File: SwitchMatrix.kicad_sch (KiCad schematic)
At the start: 130 parts, among them K1 Home, K10 A, K11 Z, K12 Alt, K13 W, K14 S, K15 X, K16 Super, K17 E, K18 D, K19 C, K2 End, K20 &dArr;, K21 R, K22 F, K23 V, K24 T, K25 G, K26 B, K27 Blank, K28 Y, K29 H, K3 Vol +, K30 N, K31 U, K32 J, K33 M, K34 &uArr;, K35 I, K36 K, K37 ,, K38 Alt, K39 O, K4 Vol -, K40 L, K41 ., K42 Fn, K43 P, K44 ;, K45 /, K46 Back Space, K47 ', K48 Shift, K49 &larr;, K5 Tab, K50 Delete, K51 Return, K52 &uarr;, K53 &darr;, K54 &rarr;, K55 1, K56 4, K57 7, K58 2, K59 5, K6 Esc, K60 8, K61 0, K62 3, K63 6, K64 9, K65 Enter, K7 Shift, K8 Ctrl, K9 Q

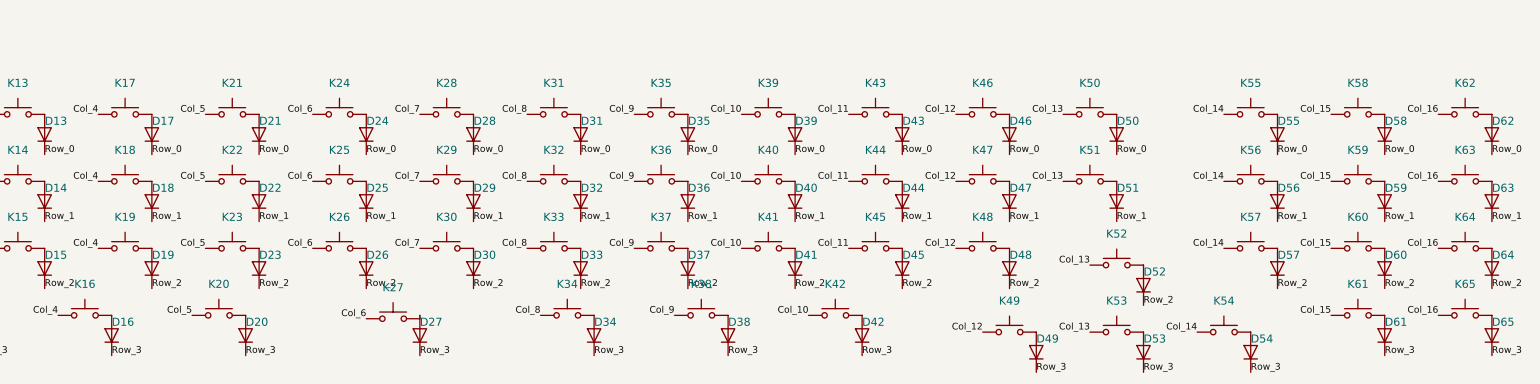
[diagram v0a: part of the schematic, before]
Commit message: layout rp2040 mwe
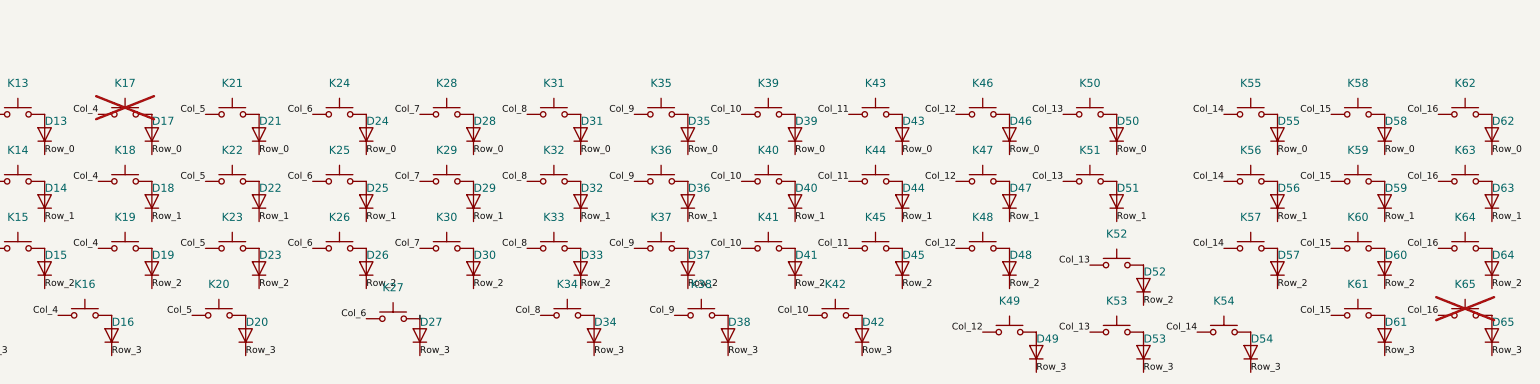
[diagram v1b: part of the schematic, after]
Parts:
- K17, K65: now not fitted; now left out of the parts list
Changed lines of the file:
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@@
 		(unit 1)
 		(exclude_from_sim no)
-		(in_bom yes)
-		(on_board yes)
-		(dnp no)
+		(in_bom no)
+		(on_board no)
+		(dnp yes)
 		(property "Reference" "K17"
 			(at 119.38 118.5418 0)
@@
 		(unit 1)
 		(exclude_from_sim no)
-		(in_bom yes)
-		(on_board yes)
-		(dnp no)
+		(in_bom no)
+		(on_board no)
+		(dnp yes)
 		(property "Reference" "K65"
 			(at 373.38 156.6418 0)

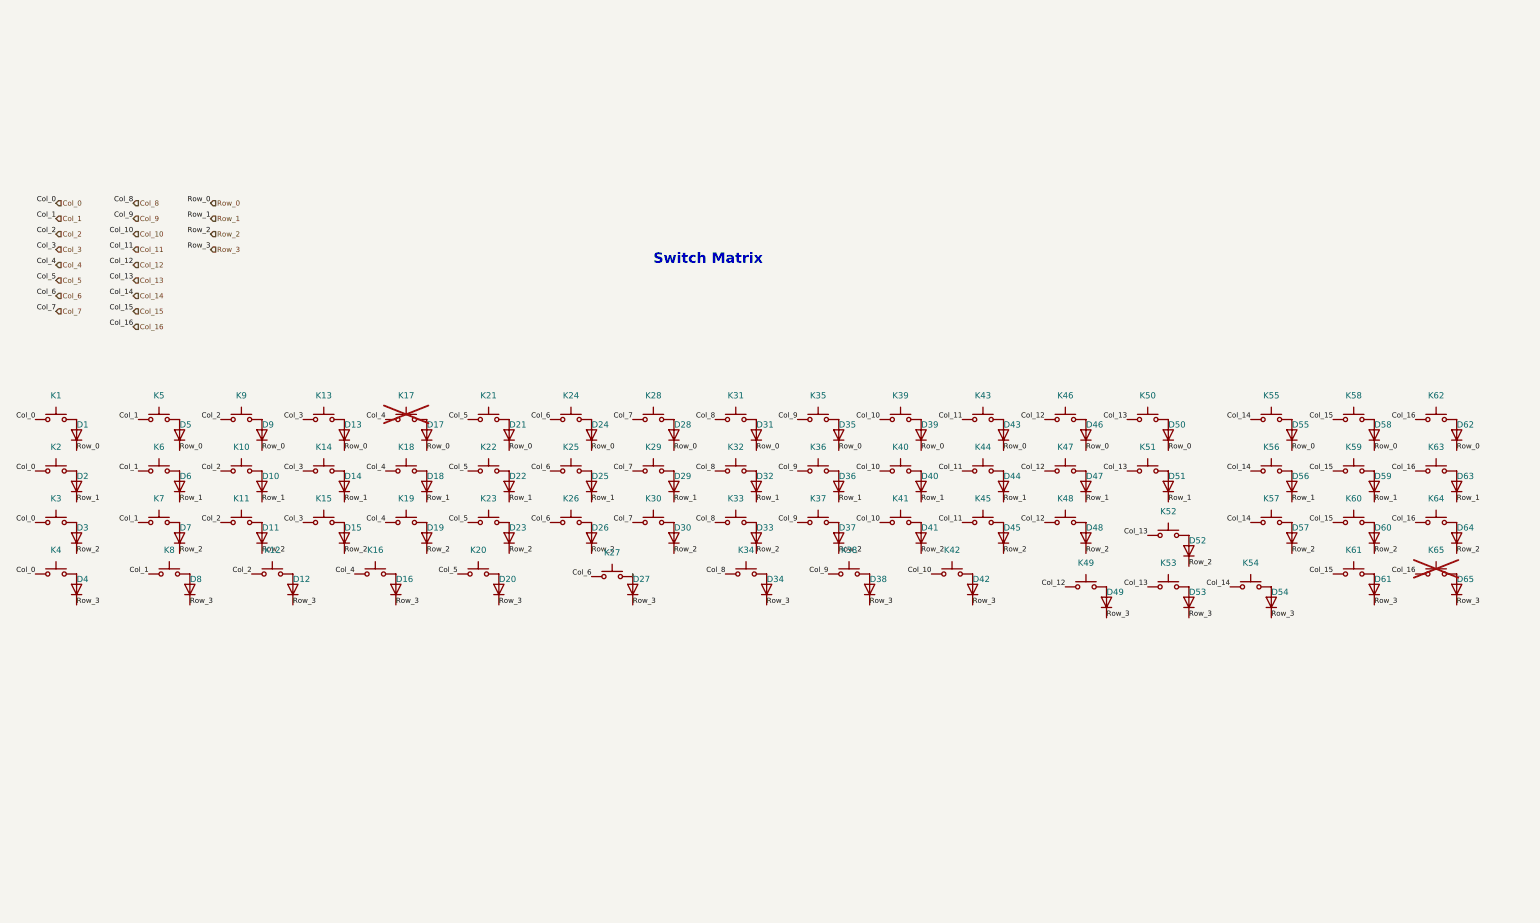
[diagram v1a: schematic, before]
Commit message: remove left most column, reroute rp2040
remove left most column, reroute rp2040 to fit in-between switches, no more oled, last 2 cols (right) are snap off. 
still to do:
- check that the snap cutouts aren't too much,
- add mounting holes for if the side is snapped off.
- still to route columns/rows
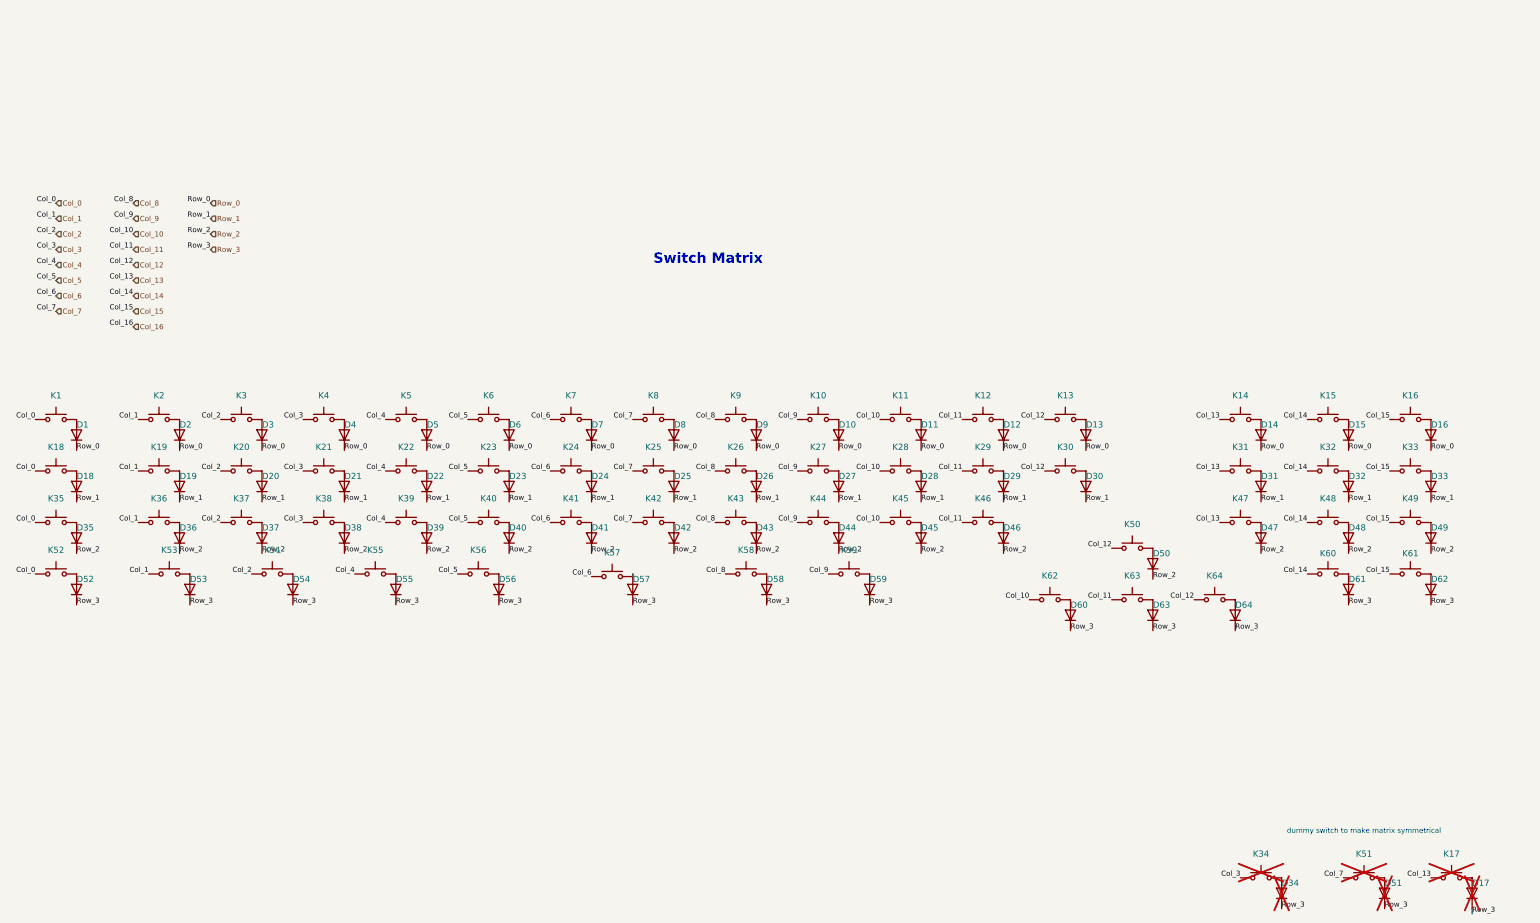
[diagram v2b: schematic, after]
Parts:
- removed D52, D54, D62, D63: D, Diode_SMD:D_0805_2012Metric_Pad1.15x1.40mm_HandSolder, symbol Device:D
- removed K52: &uarr;, PCM_Switch_Keyboard_Hotswap_Kailh:SW_Hotswap_Kailh_MX_1.00u, symbol Switch:SW_Push
- removed K54: &rarr;, PCM_Switch_Keyboard_Hotswap_Kailh:SW_Hotswap_Kailh_MX_1.00u, symbol Switch:SW_Push
- removed K62: 3, PCM_Switch_Keyboard_Hotswap_Kailh:SW_Hotswap_Kailh_MX_1.00u, symbol Switch:SW_Push
- removed K63: 6, PCM_Switch_Keyboard_Hotswap_Kailh:SW_Hotswap_Kailh_MX_1.00u, symbol Switch:SW_Push
- added D17, D34, D51: D, Diode_SMD:D_0805_2012Metric_Pad1.15x1.40mm_HandSolder, symbol Device:D
- added K17: Shift, PCM_Switch_Keyboard_Hotswap_Kailh:SW_Hotswap_Kailh_MX_1.00u, symbol Switch:SW_Push
- added K34: Super, PCM_Switch_Keyboard_Hotswap_Kailh:SW_Hotswap_Kailh_MX_1.00u, symbol Switch:SW_Push
- added K51: N, PCM_Switch_Keyboard_Hotswap_Kailh:SW_Hotswap_Kailh_MX_1.00u, symbol Switch:SW_Push
- K5: renamed from K17; now fitted; now in the parts list
- K52: renamed from K4; footprint PCM_Switch_Keyboard_Hotswap_Kailh:SW_Hotswap_Kailh_MX_1.00u -> PCM_Switch_Keyboard_Hotswap_Kailh:SW_Hotswap_Kailh_MX_1.25u
- K53: renamed from K8; footprint PCM_Switch_Keyboard_Hotswap_Kailh:SW_Hotswap_Kailh_MX_1.00u -> PCM_Switch_Keyboard_Hotswap_Kailh:SW_Hotswap_Kailh_MX_1.25u
- K54: renamed from K12; footprint PCM_Switch_Keyboard_Hotswap_Kailh:SW_Hotswap_Kailh_MX_1.00u -> PCM_Switch_Keyboard_Hotswap_Kailh:SW_Hotswap_Kailh_MX_1.25u
- K55: renamed from K16; footprint PCM_Switch_Keyboard_Hotswap_Kailh:SW_Hotswap_Kailh_MX_1.00u -> PCM_Switch_Keyboard_Hotswap_Kailh:SW_Hotswap_Kailh_MX_1.25u
- K56: renamed from K20; footprint PCM_Switch_Keyboard_Hotswap_Kailh:SW_Hotswap_Kailh_MX_1.00u -> PCM_Switch_Keyboard_Hotswap_Kailh:SW_Hotswap_Kailh_MX_1.25u
- K57: renamed from K27; footprint PCM_Switch_Keyboard_Hotswap_Kailh:SW_Hotswap_Kailh_MX_1.00u -> PCM_Switch_Keyboard_Hotswap_Kailh:SW_Hotswap_Kailh_MX_2.00u
- K58: renamed from K34; footprint PCM_Switch_Keyboard_Hotswap_Kailh:SW_Hotswap_Kailh_MX_1.00u -> PCM_Switch_Keyboard_Hotswap_Kailh:SW_Hotswap_Kailh_MX_1.25u
- K59: renamed from K38; footprint PCM_Switch_Keyboard_Hotswap_Kailh:SW_Hotswap_Kailh_MX_1.00u -> PCM_Switch_Keyboard_Hotswap_Kailh:SW_Hotswap_Kailh_MX_1.25u
- K61: renamed from K65; now fitted
- renumbered D35 to D10, D39 to D11, D43 to D12, D46 to D13, D50 to D14, D55 to D15, D58 to D16, D2 to D18, D6 to D19, D5 to D2, D10 to D20, D14 to D21, D18 to D22, D22 to D23, D25 to D24, D29 to D25, D32 to D26, D36 to D27, D40 to D28, D44 to D29, D9 to D3, D47 to D30, D51 to D31, D56 to D32, D59 to D33, D3 to D35, D7 to D36, D11 to D37, D15 to D38, D19 to D39, D13 to D4, D23 to D40, D26 to D41, D30 to D42, D33 to D43, D37 to D44, D41 to D45, D45 to D46, D48 to D47, D57 to D48, D60 to D49, D17 to D5, D64 to D50, D4 to D52, D8 to D53, D12 to D54, D16 to D55, D20 to D56, D27 to D57, D34 to D58, D38 to D59, D21 to D6, D42 to D60, D65 to D62, D49 to D63, D53 to D64, D24 to D7, D28 to D8, D31 to D9, K35 to K10, K39 to K11, K43 to K12, K46 to K13, K50 to K14, K55 to K15, K58 to K16, K2 to K18, K6 to K19, K5 to K2, K10 to K20, K14 to K21, K18 to K22, K22 to K23, K25 to K24, K29 to K25, K32 to K26, K36 to K27, K40 to K28, K44 to K29, K9 to K3, K47 to K30, K51 to K31, K56 to K32, K59 to K33, K3 to K35, K7 to K36, K11 to K37, K15 to K38, K19 to K39, K13 to K4, K23 to K40, K26 to K41, K30 to K42, K33 to K43, K37 to K44, K41 to K45, K45 to K46, K48 to K47, K57 to K48, K60 to K49, K64 to K50, K21 to K6, K61 to K60, K42 to K62, K49 to K63, K53 to K64, K24 to K7, K28 to K8, K31 to K9
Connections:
- net Col_11: now also K63.1
- net Col_12: now also K50.1, K64.1; no longer K47.1, K63.1
- net Col_13: now also K47.1, K17.1; no longer K64.1
- net Col_14: now also K60.1
- net Col_15: now also K61.1; no longer K60.1
- net Col_16: no longer K50.1, K61.1
- net Col_3: now also K34.1
- net Col_7: now also K51.1
- net Row_3: now also D17.1 (K), D34.1 (K), D51.1 (K)
- new net: D34.2 (A), K34.2
- new net: D51.2 (A), K51.2
- new net: D17.2 (A), K17.2
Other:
- note added: "dummy switch to make matrix symmetrical"
- moved on the sheet: D14, D15, D16, D31, D32, D33, D47, D48, D49, D50, D60, D61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

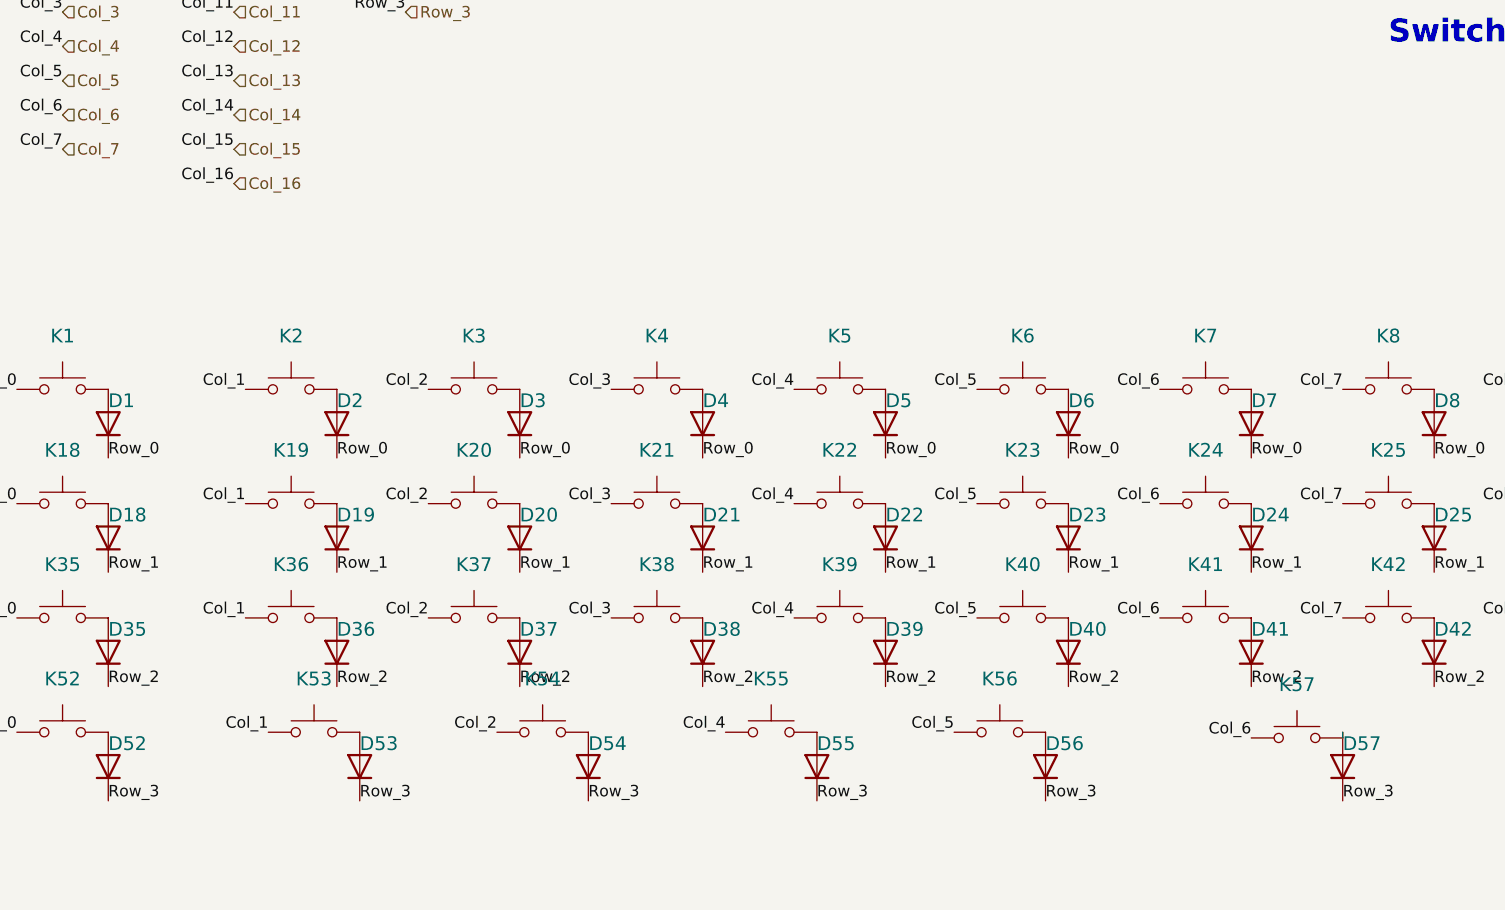
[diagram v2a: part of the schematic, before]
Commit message: routing, rotate leds to make tracks easier
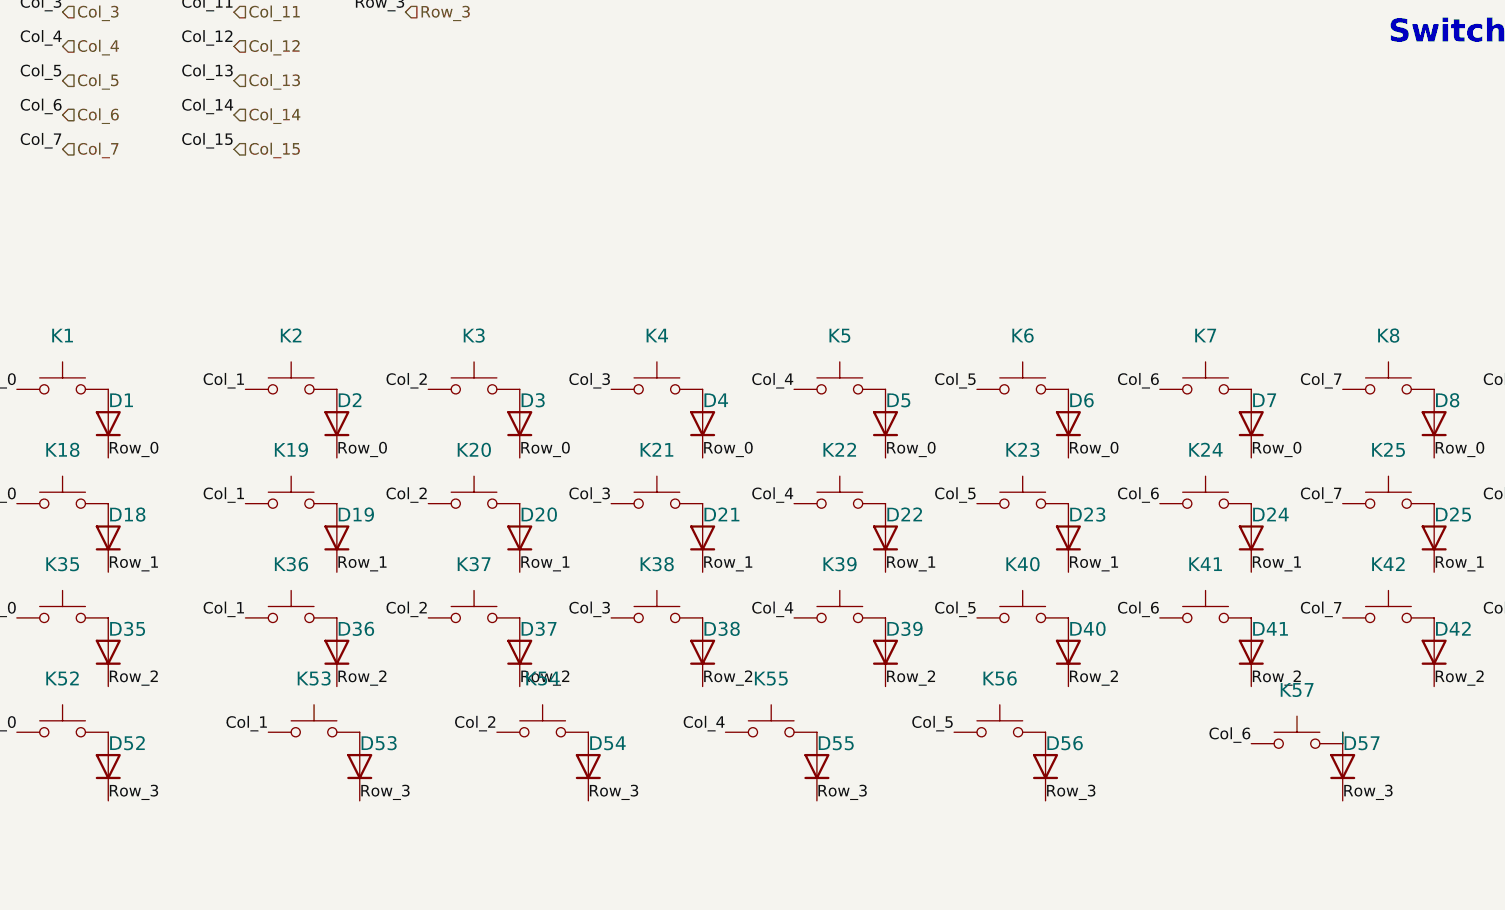
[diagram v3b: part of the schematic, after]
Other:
- moved on the sheet: K57

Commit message: pretty much done
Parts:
- added JP10, JP2, JP3, JP4, JP5, JP9: Jumper_2_Bridged, Jumper:SolderJumper-2_P1.3mm_Open_RoundedPad1.0x1.5mm, symbol Jumper:Jumper_2_Bridged
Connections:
- net Col_14: now also JP10.1 (A), JP10.2 (B)
- net Col_15: now also JP9.1 (A), JP9.2 (B)
- net Row_0: now also JP2.1 (A), JP2.2 (B)
- net Row_1: now also JP3.1 (A), JP3.2 (B)
- net Row_2: now also JP4.1 (A), JP4.2 (B)
- net Row_3: now also JP5.1 (A), JP5.2 (B)
